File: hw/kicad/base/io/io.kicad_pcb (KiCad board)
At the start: 2 copper layers, 45 x 45 mm, 10 parts, among them J1 SPI, J10 Conn_02x20_Odd_Even, J13 Conn_02x20_Odd_Even, J2 GPIO 1~4, J3 UART 2, J4 I2C, J5 GPIO 5~8, J6 CAN, J7 UART 1, J8 ADC 1~4

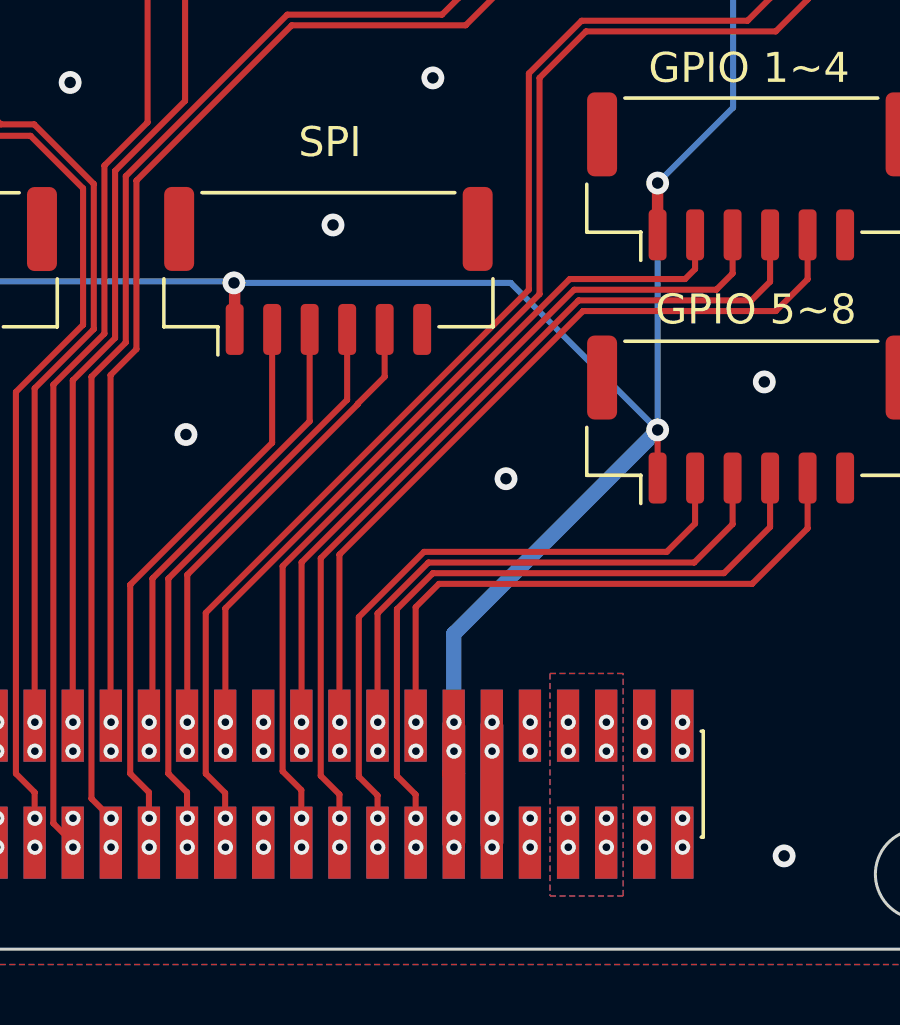
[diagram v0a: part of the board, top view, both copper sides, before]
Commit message: 增加电流传感器芯片
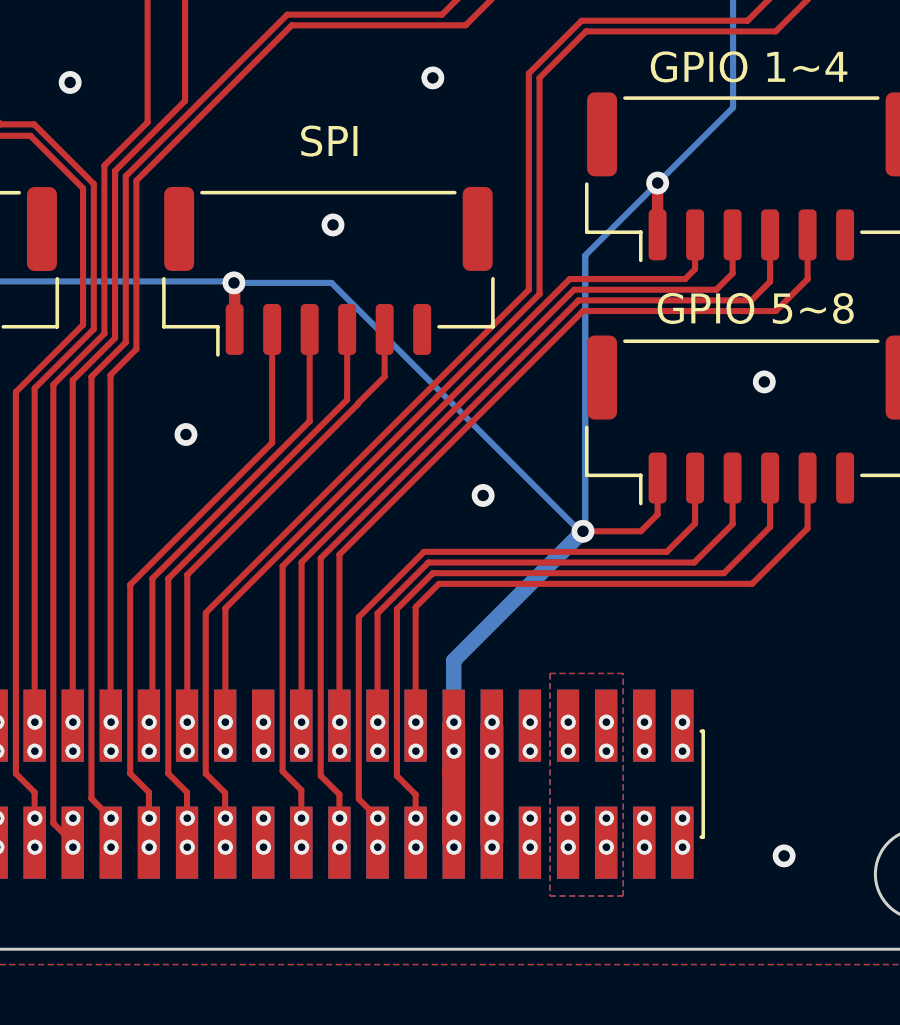
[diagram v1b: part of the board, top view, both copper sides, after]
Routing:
- net +3.3V: track 127.4 -> 128.7 mm
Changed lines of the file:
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@@
         (effects (font (size 1 1) (thickness 0.15)))
     )
-    (fp_text value "Conn_02x20_Odd_Even" (at 0 13.76 90) (layer "F.Fab")
+    (fp_text value "Conn_02x20_Odd_Even" (at 0 13.76 90) (layer "F.Fab") hide
         (effects (font (size 1 1) (thickness 0.15)))
     )
@@
         (effects (font (size 1 1) (thickness 0.15)) (justify mirror))
     )
-    (fp_text value "Conn_02x20_Odd_Even" (at 0 -13.76 90) (layer "B.Fab")
+    (fp_text value "Conn_02x20_Odd_Even" (at 0 -13.76 90) (layer "B.Fab") hide
         (effects (font (size 1 1) (thickness 0.15)) (justify mirror))
     )
@@
     (stroke (width 0.15) (type default)) (fill none) (layer "User.1"))
   (segment (start 80.5488 54.9656) (end 80.5488 53.24) (width 0.381) (layer "F.Cu") (net 1))
-  (segment (start 80.5488 61.4696) (end 80.5504 61.468) (width 0.2032) (layer "F.Cu") (net 1))
   (segment (start 80.5488 53.24) (end 80.5504 53.2384) (width 0.381) (layer "F.Cu") (net 1))
   (segment (start 83.0588 43.5926) (end 83.065 43.5864) (width 0.381) (layer "F.Cu") (net 1))
@@
   (segment (start 80.5488 62.765) (end 80.5488 63.0712) (width 0.2032) (layer "F.Cu") (net 1))
   (segment (start 72.678666 45.2774) (end 72.678666 43.741066) (width 0.381) (layer "F.Cu") (net 1))
+  (segment (start 79.9916 64.8462) (end 78.0612 64.8462) (width 0.2032) (layer "F.Cu") (net 1))
   (segment (start 66.451 58.1182) (end 66.451 56.5888) (width 0.381) (layer "F.Cu") (net 1))
   (segment (start 66.451 56.5888) (end 66.428 56.5658) (width 0.381) (layer "F.Cu") (net 1))
   (segment (start 62.298533 45.2774) (end 62.298533 43.728067) (width 0.381) (layer "F.Cu") (net 1))
+  (segment (start 80.5488 63.0712) (end 80.5488 64.289) (width 0.2032) (layer "F.Cu") (net 1))
   (segment (start 62.298533 43.728067) (end 62.3132 43.7134) (width 0.381) (layer "F.Cu") (net 1))
   (segment (start 51.9184 43.6056) (end 51.8992 43.5864) (width 0.381) (layer "F.Cu") (net 1))
   (segment (start 72.678666 43.741066) (end 72.6764 43.7388) (width 0.381) (layer "F.Cu") (net 1))
+  (segment (start 80.5488 64.289) (end 79.9916 64.8462) (width 0.2032) (layer "F.Cu") (net 1))
   (segment (start 51.9184 45.2462) (end 51.9184 43.6056) (width 0.381) (layer "F.Cu") (net 1))
   (segment (start 73.7534 71.3262) (end 73.7534 72.9234) (width 0.762) (layer "F.Cu") (net 1))
-  (segment (start 80.5488 63.0712) (end 80.5488 61.4696) (width 0.2032) (layer "F.Cu") (net 1))
   (segment (start 83.0588 45.2462) (end 83.0588 43.5926) (width 0.381) (layer "F.Cu") (net 1))
   (via (at 66.428 56.5658) (size 0.762) (drill 0.381) (layers "F.Cu" "B.Cu") (net 1))
@@
   (via (at 73.7616 72.1762) (size 0.508) (drill 0.254) (layers "F.Cu" "B.Cu") (net 1))
   (via (at 73.7616 71.211) (size 0.508) (drill 0.254) (layers "F.Cu" "B.Cu") (net 1))
-  (via (at 80.5504 61.468) (size 0.762) (drill 0.381) (layers "F.Cu" "B.Cu") (net 1))
+  (via (at 78.0612 64.8462) (size 0.762) (drill 0.381) (layers "F.Cu" "B.Cu") (net 1))
   (via (at 80.5504 53.2384) (size 0.762) (drill 0.381) (layers "F.Cu" "B.Cu") (net 1))
   (via (at 73.7616 75.3766) (size 0.508) (drill 0.254) (layers "F.Cu" "B.Cu") (net 1))
   (segment (start 83.065 43.5864) (end 72.6764 43.5864) (width 0.2032) (layer "B.Cu") (net 1))
-  (segment (start 80.5504 61.468) (end 80.5504 53.2384) (width 0.2032) (layer "B.Cu") (net 1))
-  (segment (start 66.428 56.5658) (end 75.6482 56.5658) (width 0.2032) (layer "B.Cu") (net 1))
+  (segment (start 66.428 56.5658) (end 69.6792 56.5658) (width 0.2032) (layer "B.Cu") (net 1))
+  (segment (start 73.7534 69.154) (end 78.0612 64.8462) (width 0.508) (layer "B.Cu") (net 1))
+  (segment (start 73.7534 71.3262) (end 73.7534 69.154) (width 0.508) (layer "B.Cu") (net 1))
   (segment (start 72.6764 43.5864) (end 62.3132 43.5864) (width 0.2032) (layer "B.Cu") (net 1))
   (segment (start 62.3132 43.5864) (end 51.8992 43.5864) (width 0.2032) (layer "B.Cu") (net 1))
   (segment (start 51.8992 43.5864) (end 51.8992 56.4896) (width 0.2032) (layer "B.Cu") (net 1))
   (segment (start 73.7534 71.3262) (end 73.7534 75.2262) (width 0.762) (layer "B.Cu") (net 1))
+  (segment (start 78.1374 64.77) (end 78.0612 64.8462) (width 0.2032) (layer "B.Cu") (net 1))
+  (segment (start 78.1374 55.6514) (end 78.1374 64.77) (width 0.2032) (layer "B.Cu") (net 1))
   (segment (start 80.5504 53.2384) (end 83.065 50.7238) (width 0.2032) (layer "B.Cu") (net 1))
   (segment (start 51.9246 56.515) (end 66.3772 56.515) (width 0.2032) (layer "B.Cu") (net 1))
-  (segment (start 75.6482 56.5658) (end 80.5504 61.468) (width 0.2032) (layer "B.Cu") (net 1))
-  (segment (start 73.7534 68.265) (end 80.5504 61.468) (width 0.508) (layer "B.Cu") (net 1))
+  (segment (start 80.5504 53.2384) (end 78.1374 55.6514) (width 0.2032) (layer "B.Cu") (net 1))
   (segment (start 66.3772 56.515) (end 66.428 56.5658) (width 0.2032) (layer "B.Cu") (net 1))
-  (segment (start 73.7534 71.3262) (end 73.7534 68.265) (width 0.508) (layer "B.Cu") (net 1))
   (segment (start 51.8992 56.4896) (end 51.9246 56.515) (width 0.2032) (layer "B.Cu") (net 1))
   (segment (start 83.065 50.7238) (end 83.065 43.5864) (width 0.2032) (layer "B.Cu") (net 1))
+  (segment (start 69.6792 56.5658) (end 77.9596 64.8462) (width 0.2032) (layer "B.Cu") (net 1))
+  (segment (start 77.9596 64.8462) (end 78.0612 64.8462) (width 0.2032) (layer "B.Cu") (net 1))
   (via (at 54.94085 36.6776) (size 0.762) (drill 0.381) (layers "F.Cu" "B.Cu") (net 2))
   (via (at 89.9992 63.60795) (size 0.762) (drill 0.381) (layers "F.Cu" "B.Cu") (net 2))
@@
   (via (at 84.07465 36.6776) (size 0.762) (drill 0.381) (layers "F.Cu" "B.Cu") (net 2))
   (via (at 80.1116 75.3766) (size 0.508) (drill 0.254) (layers "F.Cu" "B.Cu") (net 2))
-  (via (at 75.4958 63.0936) (size 0.762) (drill 0.381) (layers "F.Cu" "B.Cu") (net 2))
+  (via (at 74.7338 63.6524) (size 0.762) (drill 0.381) (layers "F.Cu" "B.Cu") (net 2))
   (via (at 80.1116 74.4114) (size 0.508) (drill 0.254) (layers "F.Cu" "B.Cu") (net 2))
   (via (at 84.7668 75.6666) (size 0.762) (drill 0.381) (layers "F.Cu" "B.Cu") (net 2))
@@
   (via (at 69.9516 72.1762) (size 0.508) (drill 0.254) (layers "F.Cu" "B.Cu") (net 11))
   (via (at 69.9516 71.211) (size 0.508) (drill 0.254) (layers "F.Cu" "B.Cu") (net 11))
-  (segment (start 70.5894 73.025) (end 71.2134 73.649) (width 0.2032) (layer "F.Cu") (net 12))
-  (segment (start 71.2134 73.649) (end 71.2134 75.2262) (width 0.2032) (layer "F.Cu") (net 12))
   (segment (start 81.7988 63.0712) (end 81.7988 64.5884) (width 0.2032) (layer "F.Cu") (net 12))
-  (segment (start 70.5894 67.705412) (end 70.5894 73.025) (width 0.2032) (layer "F.Cu") (net 12))
+  (segment (start 80.8552 65.532) (end 72.762812 65.532) (width 0.2032) (layer "F.Cu") (net 12))
   (segment (start 81.7988 64.5884) (end 80.8552 65.532) (width 0.2032) (layer "F.Cu") (net 12))
+  (segment (start 70.5894 73.7722) (end 71.2134 74.3962) (width 0.2032) (layer "F.Cu") (net 12))
   (segment (start 72.762812 65.532) (end 70.5894 67.705412) (width 0.2032) (layer "F.Cu") (net 12))
-  (segment (start 80.8552 65.532) (end 72.762812 65.532) (width 0.2032) (layer "F.Cu") (net 12))
+  (segment (start 71.2134 74.3962) (end 71.2134 75.2262) (width 0.2032) (layer "F.Cu") (net 12))
+  (segment (start 70.5894 67.705412) (end 70.5894 73.7722) (width 0.2032) (layer "F.Cu") (net 12))
   (via (at 71.2216 75.3766) (size 0.508) (drill 0.254) (layers "F.Cu" "B.Cu") (net 12))
   (via (at 71.2216 74.4114) (size 0.508) (drill 0.254) (layers "F.Cu" "B.Cu") (net 12))
